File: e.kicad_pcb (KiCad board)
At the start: 2 copper layers, 69.8 x 81.6 mm, 8 parts, among them SW1 SW_Push, SW2 SW_Push, U2 MAX98357A

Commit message: i did MORE things
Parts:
- SW1: value SW_Push -> pwr
- SW2: value SW_Push -> rst
- moved SW1 61.0 mm to (159.9, 137.1), turned to -90 degrees
- moved BT1 57.8 mm to (112.9, 112.1), turned to -90 degrees
- moved R1 52.0 mm to (159.6, 128.1), turned to -90 degrees
- moved SW2 41.4 mm to (162.9, 115.9), turned to 90 degrees
- moved A1 28.4 mm to (142.6, 111.7)
- moved U2 23.5 mm to (123.2, 94.5), turned to 180 degrees
- moved D2 18.0 mm to (159.5, 91.1), turned to 90 degrees
- moved R2 14.7 mm to (123.1, 88.4), turned to 90 degrees
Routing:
- net Net-(A1-GPIO16): track 0.00 -> 16.2 mm
- net Net-(A1-GPIO0): track 0.00 -> 11.1 mm
- net Net-(A1-GPIO1): track 0.00 -> 10.2 mm
- net Net-(A1-VSYS): track 0.00 -> 9.30 mm
- net Net-(A1-GPIO2): track 0.00 -> 8.34 mm
- net GND: track 0.00 -> 8.17 mm
- net Net-(U2-GAIN_SLOT): track 0.00 -> 4.55 mm
- removed copper zone on B.Cu, net GND
- removed copper zone on F.Cu, net GND
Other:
- board size 69.8 x 81.6 mm -> 97.3 x 62.5 mm
- board text added: "click me!! <---"
- board text added: "made by montypythonist X3"
- board text added: "some notes: insert words here :)"

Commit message: its all doom and despair from here on out
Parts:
- added LS1: Speaker, stupid-dumb-speaker:stupid-dumb-speaker, F.Cu at (192.1, 135.1)
- added U1: ~, display-lol:display-lol, F.Cu at (195.4, 89.0)
- SW1: value pwr -> usr
- moved SW1 68.7 mm to (227.1, 151.6), turned to 0 degrees
- moved SW2 65.2 mm to (227.9, 120.4)
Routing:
- net Net-(U2-OUTN): track 0.00 -> 114.0 mm
- net Net-(A1-RUN): track 0.00 -> 97.8 mm
- net Net-(A1-GPIO16): track 16.2 -> 107.6 mm
- net Net-(A1-GPIO22): track 0.00 -> 60.4 mm
- net Net-(A1-GPIO21): track 0.00 -> 57.1 mm
- net Net-(A1-GPIO20): track 0.00 -> 52.8 mm
- net Net-(A1-GPIO19): track 0.00 -> 50.9 mm
- net Net-(A1-GPIO17): track 0.00 -> 50.1 mm
- net Net-(A1-GPIO18): track 0.00 -> 49.9 mm
- net +3V0: track 0.00 -> 29.7 mm
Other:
- board size 97.3 x 62.5 mm -> 136.8 x 92.5 mm
- board text added: "this routing haunts me in my sleep"

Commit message: i rembered to put the ground plane this time trust
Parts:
- SW1, SW2: footprint Button_Switch_SMD:SW_SPST_B3U-3100P-B -> Button_Switch_SMD:SW_SPST_B3S-1000
- moved SW2 5.33 mm to (225.5, 115.7), turned to 0 degrees
- moved SW1 2.48 mm to (225.0, 150.2)
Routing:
- net Net-(A1-RUN): track 97.8 -> 92.0 mm
- net Net-(A1-GPIO16): track 107.6 -> 102.1 mm
- added copper zone on B.Cu, net GND
- added copper zone on F.Cu, net GND

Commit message: omg yay pcb fully made and its amazing and beautiful and the DRC errors make no sense :3
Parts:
- SW1: footprint Button_Switch_SMD:SW_SPST_B3S-1000 -> Button_Switch_THT:SW_Slide_SPDT_Straight_CK_OS102011MS2Q
- U1: value ~ -> Display_ST7789
- U2: footprint Package_DFN_QFN:TQFN-16-1EP_3x3mm_P0.5mm_EP1.23x1.23mm -> MAX98357A:MAX98357A
- moved SW2 78.3 mm to (148.5, 101.7)
- moved SW1 71.8 mm to (190.0, 87.5), turned to -90 degrees
- moved U1 50.1 mm to (174.4, 134.5)
- moved R1 41.4 mm to (200.6, 122.6)
- moved R2 40.5 mm to (91.6, 113.9)
- moved LS1 37.5 mm to (172.6, 103.1)
- moved D2 26.2 mm to (146.0, 113.6), turned to -90 degrees
- moved BT1 23.5 mm to (103.4, 133.6)
- moved U2 23.2 mm to (100.5, 99.2), turned to 90 degrees
- moved A1 15.9 mm to (130.6, 122.2)
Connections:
- SW1 pad 1: Net-(A1-GPIO16) -> GND
- SW1 pad 2: GND -> Net-(A1-GPIO16)
- U2 pad 8: +3V0 -> Net-(U2-OUTP)
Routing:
- net Net-(U2-OUTP): track 0.00 -> 90.4 mm
- net Net-(U2-OUTN): track 114.0 -> 76.1 mm
- net Net-(A1-GPIO16): track 102.1 -> 138.7 mm
- net +3V0: track 29.7 -> 0.00 mm
- net Net-(U2-GAIN_SLOT): track 4.55 -> 29.1 mm
- net Net-(A1-GPIO17): track 50.1 -> 32.0 mm
- net Net-(A1-GPIO18): track 49.9 -> 35.8 mm
- net Net-(A1-GPIO19): track 50.9 -> 39.4 mm
- net Net-(A1-GPIO20): track 52.8 -> 43.0 mm
- net GND: track 8.17 -> 0.00 mm
- net Net-(A1-GPIO21): track 57.1 -> 49.1 mm
- net Net-(A1-VSYS): track 9.30 -> 14.4 mm
- net Net-(A1-GPIO2): track 8.34 -> 13.3 mm
- net Net-(A1-GPIO22): track 60.4 -> 56.3 mm
- net Net-(A1-GPIO1): track 10.2 -> 14.3 mm
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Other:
- board size 136.8 x 92.5 mm -> 115.5 x 81 mm
- board text added: "off"
- board text added: "on"
- board text added: "this routing haunts me in my sleep ^^^"
- board text added: "toggle me!! -------->"
- board text removed: "click me!! <---"
- board text removed: "this routing haunts me in my sleep"

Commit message: fixed so many things (i hope)
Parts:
- U2: footprint MAX98357A:MAX98357A -> amp-of-doom:MAX98357A
- moved BT1 101.3 mm to (190.0, 81.0), turned to 90 degrees
- moved U1 90.2 mm to (116.0, 65.8)
- moved LS1 66.6 mm to (106.0, 103.3), turned to 90 degrees
- moved D2 57.6 mm to (176.9, 65.0), turned to 0 degrees
- moved SW2 54.9 mm to (175.4, 53.8)
- moved R2 52.9 mm to (144.5, 112.0), turned to 0 degrees
- moved A1 46.5 mm to (160.4, 86.4)
- moved U2 33.8 mm to (134.2, 98.8)
- moved R1 24.3 mm to (179.0, 111.5), turned to 0 degrees
- moved SW1 20.0 mm to (179.5, 104.5), turned to 0 degrees
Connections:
- A1 pad 17: unconnected-(A1-GPIO13-Pad17)_1 -> Net-(A1-GPIO13)
- A1 pad 19: unconnected-(A1-GPIO14-Pad19)_1 -> Net-(A1-GPIO14)
- A1 pad 20: unconnected-(A1-GPIO15-Pad20) -> Net-(A1-GPIO15)
- A1 pad 22: Net-(A1-GPIO17) -> unconnected-(A1-GPIO17-Pad22)
- A1 pad 24: Net-(A1-GPIO18) -> unconnected-(A1-GPIO18-Pad24)
- A1 pad 25: Net-(A1-GPIO19) -> unconnected-(A1-GPIO19-Pad25)
- A1 pad 26: Net-(A1-GPIO20) -> unconnected-(A1-GPIO20-Pad26)
- A1 pad 27: Net-(A1-GPIO21) -> unconnected-(A1-GPIO21-Pad27)
- A1 pad 29: Net-(A1-GPIO22) -> unconnected-(A1-GPIO22-Pad29)
- A1 pad 5: unconnected-(A1-GPIO3-Pad5)_1 -> Net-(A1-GPIO3)
- A1 pad 6: unconnected-(A1-GPIO4-Pad6)_1 -> Net-(A1-GPIO4)
- A1 pad 7: unconnected-(A1-GPIO5-Pad7)_1 -> Net-(A1-GPIO5)
- A1 pad 9: unconnected-(A1-GPIO6-Pad9) -> Net-(A1-GPIO6)
- SW2 pad 1: GND -> Net-(A1-RUN)
- SW2 pad 2: Net-(A1-RUN) -> GND
- U1 pad 11: Net-(A1-GPIO22) -> Net-(A1-GPIO5)
- U1 pad 12: (no net) -> Net-(A1-GPIO6)
- U1 pad 4: Net-(A1-GPIO17) -> Net-(A1-GPIO0)
- U1 pad 5: Net-(A1-GPIO18) -> Net-(A1-GPIO1)
- U1 pad 6: Net-(A1-GPIO19) -> Net-(A1-GPIO2)
- U1 pad 7: Net-(A1-GPIO20) -> Net-(A1-GPIO3)
- U1 pad 9: Net-(A1-GPIO21) -> Net-(A1-GPIO4)
- U2 pad 1: Net-(A1-GPIO2) -> Net-(A1-GPIO15)
- U2 pad 2: Net-(A1-GPIO1) -> Net-(A1-GPIO14)
- U2 pad 3: Net-(A1-GPIO0) -> Net-(A1-GPIO13)
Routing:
- net Net-(A1-GPIO16): track 138.7 -> 19.1 mm, vias 0 -> 1
- net Net-(U2-OUTP): track 90.4 -> 22.5 mm
- net Net-(A1-GPIO22): track 56.3 -> 0.00 mm
- net Net-(U2-OUTN): track 76.1 -> 26.4 mm
- net Net-(A1-GPIO21): track 49.1 -> 0.00 mm
- net Net-(A1-GPIO20): track 43.0 -> 0.00 mm
- net Net-(A1-RUN): track 91.3 -> 133.8 mm
- net Net-(A1-GPIO19): track 39.4 -> 0.00 mm
- net Net-(A1-GPIO3): track 0.00 -> 37.4 mm
- net Net-(A1-GPIO18): track 35.8 -> 0.00 mm
- net Net-(A1-GPIO0): track 14.3 -> 49.2 mm
- net Net-(A1-GPIO17): track 32.0 -> 0.00 mm
- net Net-(A1-GPIO1): track 14.3 -> 45.6 mm
- net Net-(A1-GPIO4): track 0.00 -> 31.2 mm
- net Net-(U2-GAIN_SLOT): track 29.1 -> 0.00 mm
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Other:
- board size 115.5 x 81 mm -> 115.2 x 78.2 mm
- board text added: "<ö>"
- board text added: "this routing haunts me in my sleep"
- board text added: "toggle me!! <------"
- board text removed: "this routing haunts me in my sleep ^^^"
- board text removed: "toggle me!! -------->"

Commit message: :)
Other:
- board text removed: "<ö>"
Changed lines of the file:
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@@
-		)
-	)
-	(gr_text "<ö>"
-		(at 194 93 90)
-		(layer "F.SilkS")
-		(effects
-			(font
-				(size 0.7 0.7)
-				(thickness 0.1)
-				(bold yes)
-			)
-			(justify left bottom)
 		)
 	)

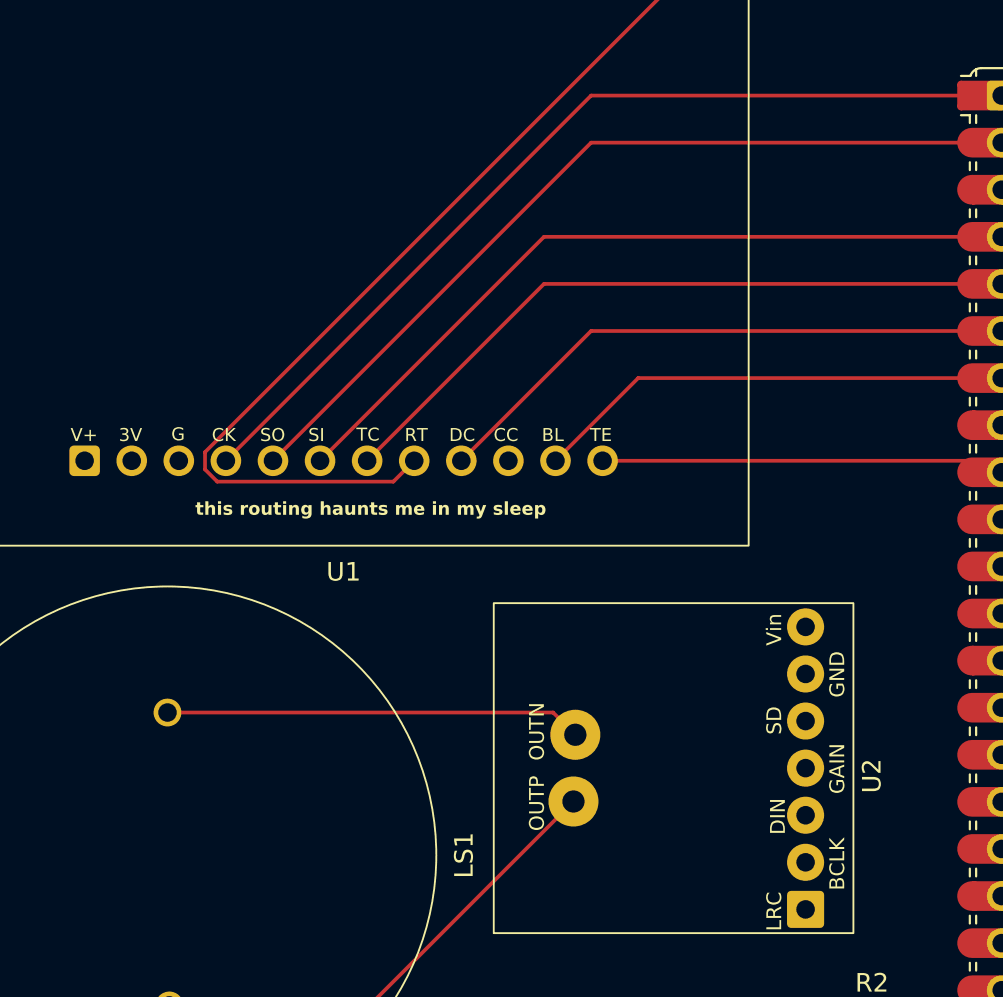
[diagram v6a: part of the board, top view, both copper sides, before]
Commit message: Updated footprint library path for custom footprints
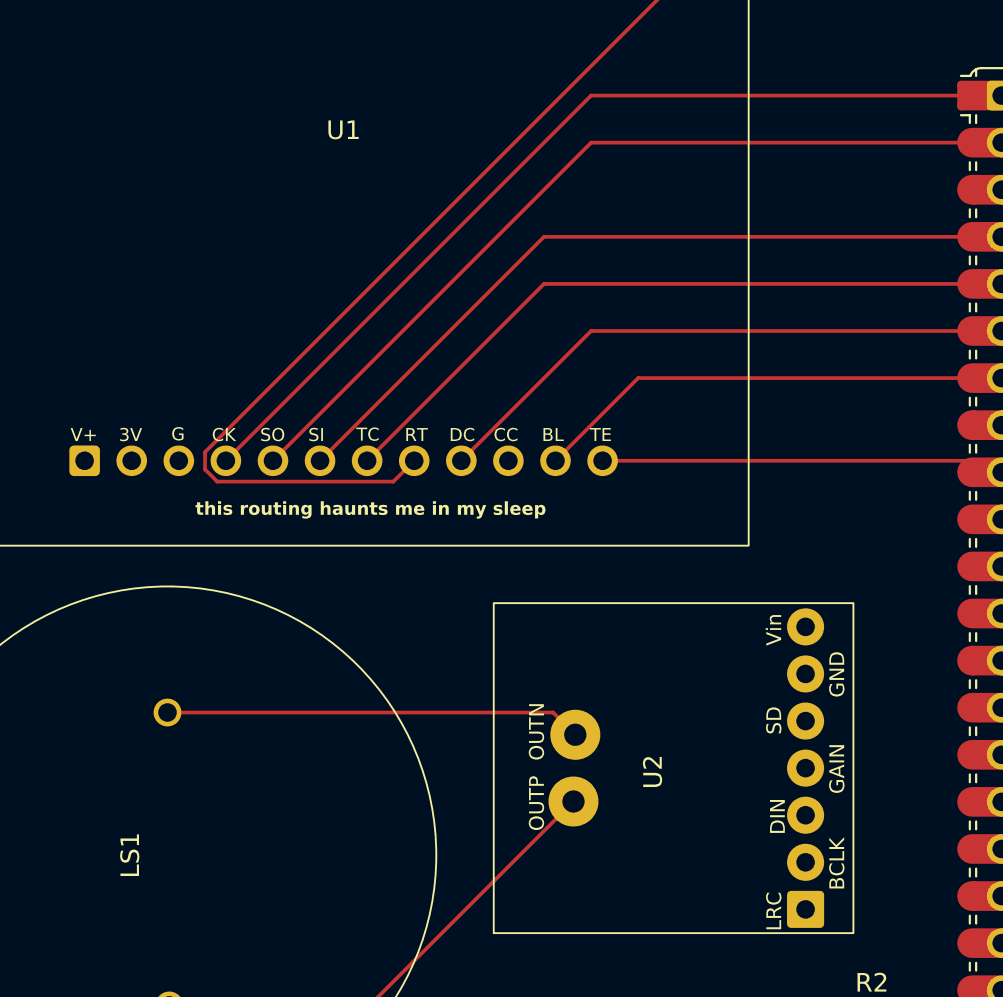
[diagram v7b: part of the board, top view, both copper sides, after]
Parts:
- LS1: footprint stupid-dumb-speaker:stupid-dumb-speaker -> custom-fp:stupid-dumb-speaker
- U1: footprint display-lol:display-lol -> custom-fp:display-lol
- U2: footprint amp-of-doom:MAX98357A -> custom-fp:MAX98357A
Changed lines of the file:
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@@
 		)
 	)
-	(footprint "amp-of-doom:MAX98357A"
+	(footprint "custom-fp:MAX98357A"
 		(layer "F.Cu")
 		(at 134.2 98.78 90)
 		(property "Reference" "U2"
-			(at -0.22 10.3 90)
+			(at 0 -1.5 90)
 			(unlocked yes)
 			(layer "F.SilkS")
@@
 		(sheetname "/")
 		(sheetfile "e.kicad_sch")
+		(units
+			(unit
+				(name "A")
+				(pins "3" "2" "1" "5" "4" "7" "6" "8" "9")
+			)
+		)
 		(attr smd)
 		(duplicate_pad_numbers_are_jumpers no)
@@
 		(embedded_fonts no)
 	)
-	(footprint "stupid-dumb-speaker:stupid-dumb-speaker"
+	(footprint "custom-fp:stupid-dumb-speaker"
 		(layer "F.Cu")
 		(at 106 103.28 90)
 		(property "Reference" "LS1"
-			(at 0 16.5 90)
+			(at 0 -1.5 90)
 			(unlocked yes)
 			(layer "F.SilkS")
@@
 		(sheetname "/")
 		(sheetfile "e.kicad_sch")
+		(units
+			(unit
+				(name "A")
+				(pins "1" "2")
+			)
+		)
 		(attr smd)
 		(duplicate_pad_numbers_are_jumpers no)
@@
 		(embedded_fonts no)
 	)
-	(footprint "display-lol:display-lol"
+	(footprint "custom-fp:display-lol"
 		(layer "F.Cu")
 		(at 116 65.78)
 		(property "Reference" "U1"
-			(at 0 22.22 0)
+			(at 0 -1.6 0)
 			(unlocked yes)
 			(layer "F.SilkS")
@@
 		(sheetname "/")
 		(sheetfile "e.kicad_sch")
+		(units
+			(unit
+				(name "A")
+				(pins "1" "3" "2" "4" "5" "6" "7" "8" "9" "10" "11" "12")
+			)
+		)
 		(attr smd)
 		(duplicate_pad_numbers_are_jumpers no)
@@
 				(name "A")
 				(pins "30" "37" "1" "2" "4" "5" "6" "7" "9" "10" "11" "12" "14" "15"
-					"16" "17" "19" "20" "39" "40" "18" "23" "28" "13" "8" "38" "3" "36"
+					"16" "17" "19" "20" "39" "40" "23" "3" "8" "38" "13" "28" "18" "36"
 					"21" "22" "24" "25" "26" "27" "29" "35" "31" "32" "34" "33"
 				)
